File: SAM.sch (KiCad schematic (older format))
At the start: 63 parts

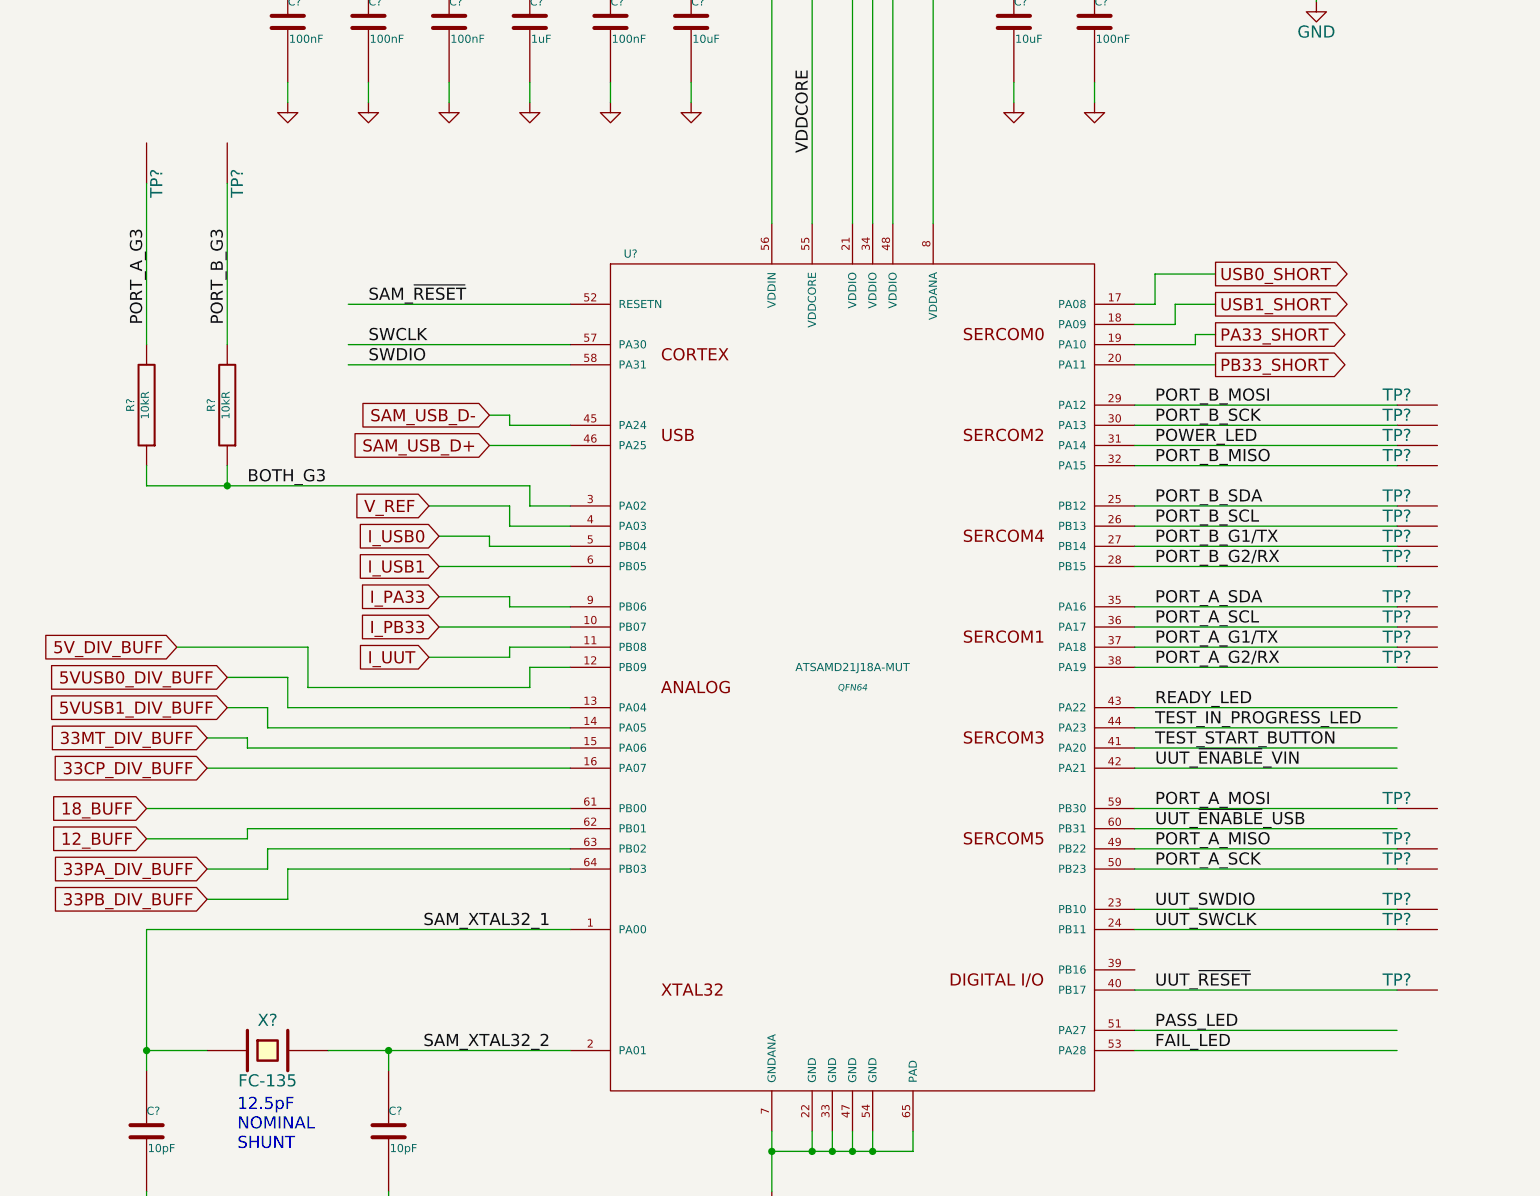
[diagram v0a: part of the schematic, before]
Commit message: added testpoint part number, small net naming changes
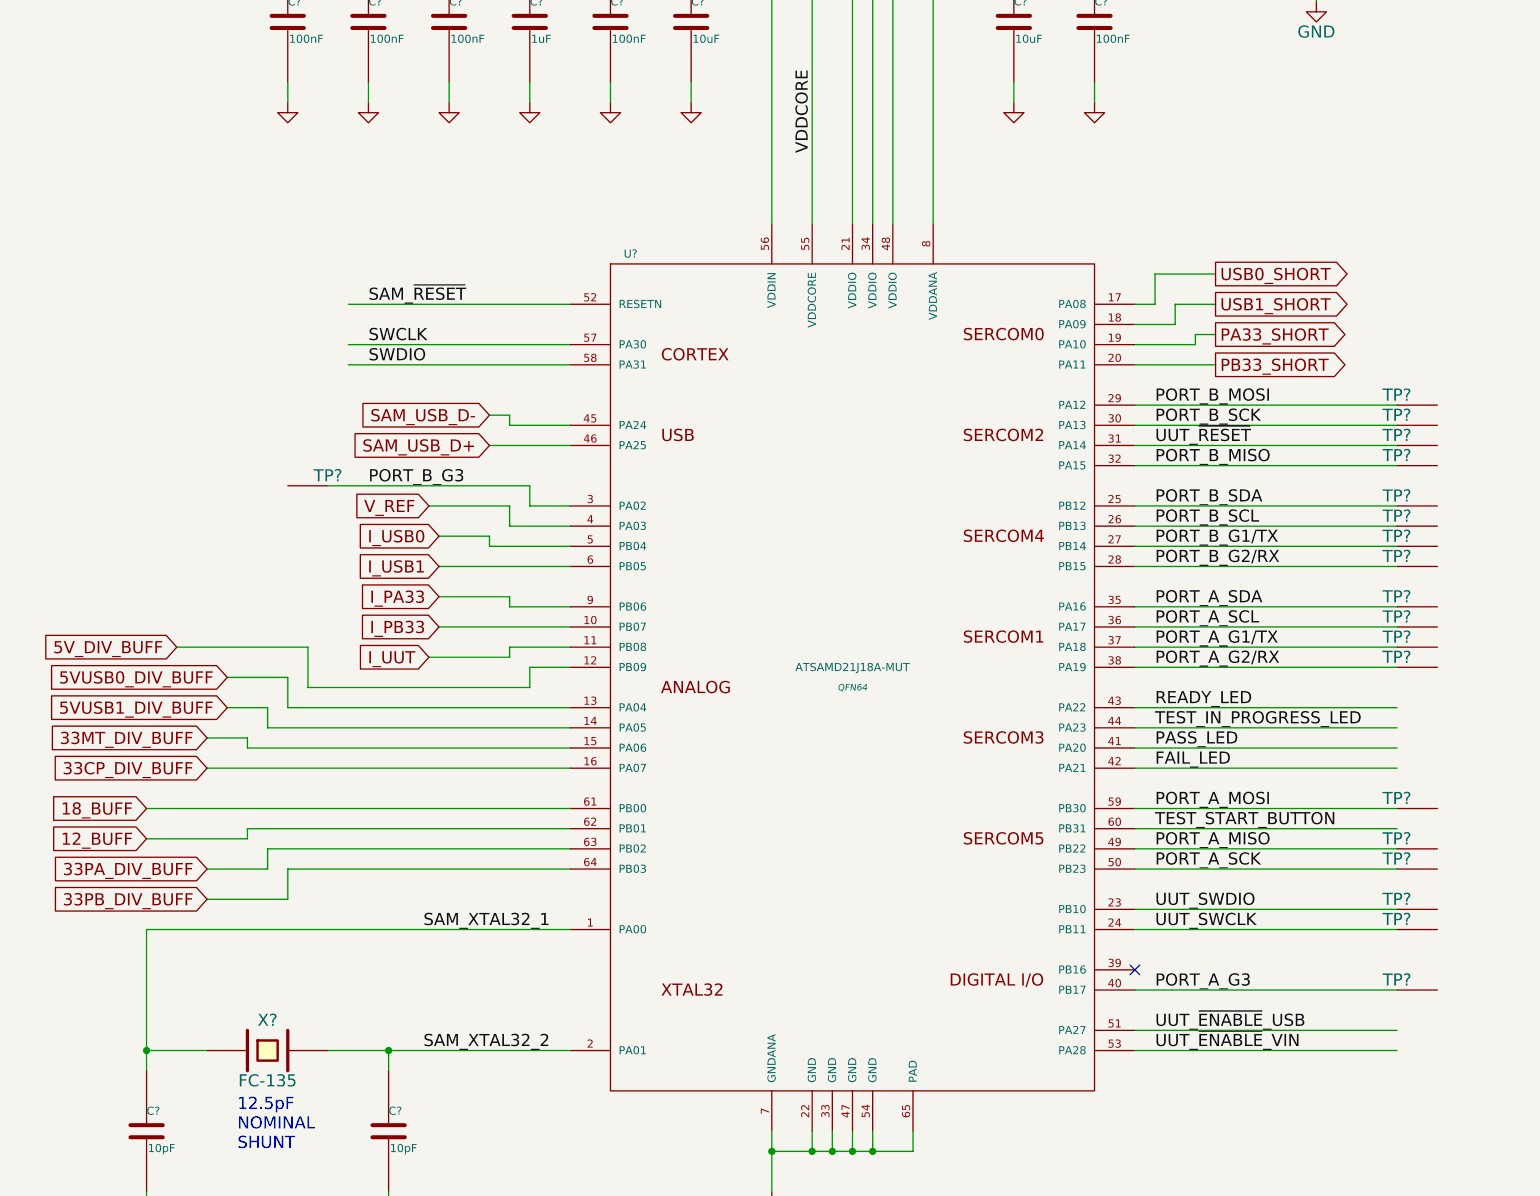
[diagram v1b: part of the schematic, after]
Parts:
- removed R? (x2): 10kR, tm-kicad-lib:SMD-0402-R, symbol TM_R
- removed TP?: TP, tm-kicad-lib:Testpoint, symbol TP
- TP? (x23): value TP -> 0914-0-15-20-77-14-11-0
- TP?: value TP -> 0914-0-15-20-77-14-11-0-0-15-20-77-14-11-0
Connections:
- net labels removed: BOTH_G3, POWER_LED
- wire segments 246 -> 241
- no-connect marks 4 -> 5
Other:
- moved on the sheet: TP?
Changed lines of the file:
@@
 Text Label 6800 6300 0    60   ~ 0
 PORT_B_G2/RX
-Text Label 2200 5100 1    60   ~ 0
+Text Label 2900 5900 0    60   ~ 0
 PORT_B_G3
 Text Label 6800 7500 0    60   ~ 0
@@
 Text Label 6800 6800 0    60   ~ 0
 PORT_A_G2/RX
-Text Label 6800 5700 0    60   ~ 0
-POWER_LED
 Text Notes 2250 9200 0    60   ~ 0
 12.5pF\nNOMINAL\nSHUNT
@@
 P 8800 2300
 F 0 "TP?" H 8800 2350 60  0000 C CNN
-F 1 "TP" H 8800 2250 60  0001 C CNN
+F 1 "0914-0-15-20-77-14-11-0" H 8800 2250 60  0001 C CNN
 F 2 "tm-kicad-lib:Testpoint" H 8800 2300 60  0001 C CNN
 F 3 "" H 8800 2300 60  0000 C CNN
@@
 P 8800 2500
 F 0 "TP?" H 8800 2550 60  0000 C CNN
-F 1 "TP" H 8800 2450 60  0001 C CNN
+F 1 "0914-0-15-20-77-14-11-0" H 8800 2450 60  0001 C CNN
 F 2 "tm-kicad-lib:Testpoint" H 8800 2500 60  0001 C CNN
 F 3 "" H 8800 2500 60  0000 C CNN
@@
 P 8800 2100
 F 0 "TP?" H 8800 2150 60  0000 C CNN
-F 1 "TP" H 8800 2050 60  0001 C CNN
+F 1 "0914-0-15-20-77-14-11-0" H 8800 2050 60  0001 C CNN
 F 2 "tm-kicad-lib:Testpoint" H 8800 2100 60  0001 C CNN
 F 3 "" H 8800 2100 60  0000 C CNN
@@
 P 8800 1900
 F 0 "TP?" H 8800 1950 60  0000 C CNN
-F 1 "TP" H 8800 1850 60  0001 C CNN
+F 1 "0914-0-15-20-77-14-11-0" H 8800 1850 60  0001 C CNN
 F 2 "tm-kicad-lib:Testpoint" H 8800 1900 60  0001 C CNN
 F 3 "" H 8800 1900 60  0000 C CNN
@@
 P 8000 5500
 F 0 "TP?" H 8000 5550 60  0000 C CNN
-F 1 "TP" H 8000 5450 60  0001 C CNN
+F 1 "0914-0-15-20-77-14-11-0-0-15-20-77-14-11-0" H 8000 5450 60  0001 C CNN
 F 2 "tm-kicad-lib:Testpoint" H 8000 5500 60  0001 C CNN
 F 3 "" H 8000 5500 60  0000 C CNN
@@
 P 8000 5600
 F 0 "TP?" H 8000 5650 60  0000 C CNN
-F 1 "TP" H 8000 5550 60  0001 C CNN
+F 1 "0914-0-15-20-77-14-11-0" H 8000 5550 60  0001 C CNN
 F 2 "tm-kicad-lib:Testpoint" H 8000 5600 60  0001 C CNN
 F 3 "" H 8000 5600 60  0000 C CNN
@@
 $Comp
 L TP TP?
-U 1 1 553FEFB0
-P 8000 5700
-F 0 "TP?" H 8000 5750 60  0000 C CNN
-F 1 "TP" H 8000 5650 60  0001 C CNN
-F 2 "tm-kicad-lib:Testpoint" H 8000 5700 60  0001 C CNN
-F 3 "" H 8000 5700 60  0000 C CNN
-	1    8000 5700
-	1    0    0    -1
-$EndComp
-$Comp
-L TP TP?
 U 1 1 553FEFB6
 P 8000 5800
 F 0 "TP?" H 8000 5850 60  0000 C CNN
-F 1 "TP" H 8000 5750 60  0001 C CNN
+F 1 "0914-0-15-20-77-14-11-0" H 8000 5750 60  0001 C CNN
 F 2 "tm-kicad-lib:Testpoint" H 8000 5800 60  0001 C CNN
 F 3 "" H 8000 5800 60  0000 C CNN
@@
 P 8000 6000
 F 0 "TP?" H 8000 6050 60  0000 C CNN
-F 1 "TP" H 8000 5950 60  0001 C CNN
+F 1 "0914-0-15-20-77-14-11-0" H 8000 5950 60  0001 C CNN
 F 2 "tm-kicad-lib:Testpoint" H 8000 6000 60  0001 C CNN
 F 3 "" H 8000 6000 60  0000 C CNN
@@
 P 8000 6100
 F 0 "TP?" H 8000 6150 60  0000 C CNN
-F 1 "TP" H 8000 6050 60  0001 C CNN
+F 1 "0914-0-15-20-77-14-11-0" H 8000 6050 60  0001 C CNN
 F 2 "tm-kicad-lib:Testpoint" H 8000 6100 60  0001 C CNN
 F 3 "" H 8000 6100 60  0000 C CNN
@@
 P 8000 6200
 F 0 "TP?" H 8000 6250 60  0000 C CNN
-F 1 "TP" H 8000 6150 60  0001 C CNN
+F 1 "0914-0-15-20-77-14-11-0" H 8000 6150 60  0001 C CNN
 F 2 "tm-kicad-lib:Testpoint" H 8000 6200 60  0001 C CNN
 F 3 "" H 8000 6200 60  0000 C CNN
@@
 P 8000 6300
 F 0 "TP?" H 8000 6350 60  0000 C CNN
-F 1 "TP" H 8000 6250 60  0001 C CNN
+F 1 "0914-0-15-20-77-14-11-0" H 8000 6250 60  0001 C CNN
 F 2 "tm-kicad-lib:Testpoint" H 8000 6300 60  0001 C CNN
 F 3 "" H 8000 6300 60  0000 C CNN
@@
 P 8000 6500
 F 0 "TP?" H 8000 6550 60  0000 C CNN
-F 1 "TP" H 8000 6450 60  0001 C CNN
+F 1 "0914-0-15-20-77-14-11-0" H 8000 6450 60  0001 C CNN
 F 2 "tm-kicad-lib:Testpoint" H 8000 6500 60  0001 C CNN
 F 3 "" H 8000 6500 60  0000 C CNN
@@
 P 8000 6600
 F 0 "TP?" H 8000 6650 60  0000 C CNN
-F 1 "TP" H 8000 6550 60  0001 C CNN
+F 1 "0914-0-15-20-77-14-11-0" H 8000 6550 60  0001 C CNN
 F 2 "tm-kicad-lib:Testpoint" H 8000 6600 60  0001 C CNN
 F 3 "" H 8000 6600 60  0000 C CNN
@@
 P 8000 6700
 F 0 "TP?" H 8000 6750 60  0000 C CNN
-F 1 "TP" H 8000 6650 60  0001 C CNN
+F 1 "0914-0-15-20-77-14-11-0" H 8000 6650 60  0001 C CNN
 F 2 "tm-kicad-lib:Testpoint" H 8000 6700 60  0001 C CNN
 F 3 "" H 8000 6700 60  0000 C CNN
@@
 P 8000 6800
 F 0 "TP?" H 8000 6850 60  0000 C CNN
-F 1 "TP" H 8000 6750 60  0001 C CNN
+F 1 "0914-0-15-20-77-14-11-0" H 8000 6750 60  0001 C CNN
 F 2 "tm-kicad-lib:Testpoint" H 8000 6800 60  0001 C CNN
 F 3 "" H 8000 6800 60  0000 C CNN
@@
 P 8000 8000
 F 0 "TP?" H 8000 8050 60  0000 C CNN
-F 1 "TP" H 8000 7950 60  0001 C CNN
+F 1 "0914-0-15-20-77-14-11-0" H 8000 7950 60  0001 C CNN
 F 2 "tm-kicad-lib:Testpoint" H 8000 8000 60  0001 C CNN
 F 3 "" H 8000 8000 60  0000 C CNN
@@
 P 8000 8100
 F 0 "TP?" H 8000 8150 60  0000 C CNN
-F 1 "TP" H 8000 8050 60  0001 C CNN
+F 1 "0914-0-15-20-77-14-11-0" H 8000 8050 60  0001 C CNN
 F 2 "tm-kicad-lib:Testpoint" H 8000 8100 60  0001 C CNN
 F 3 "" H 8000 8100 60  0000 C CNN
@@
 P 8000 7700
 F 0 "TP?" H 8000 7750 60  0000 C CNN
-F 1 "TP" H 8000 7650 60  0001 C CNN
+F 1 "0914-0-15-20-77-14-11-0" H 8000 7650 60  0001 C CNN
 F 2 "tm-kicad-lib:Testpoint" H 8000 7700 60  0001 C CNN
 F 3 "" H 8000 7700 60  0000 C CNN
@@
 P 8000 7800
 F 0 "TP?" H 8000 7850 60  0000 C CNN
-F 1 "TP" H 8000 7750 60  0001 C CNN
+F 1 "0914-0-15-20-77-14-11-0" H 8000 7750 60  0001 C CNN
 F 2 "tm-kicad-lib:Testpoint" H 8000 7800 60  0001 C CNN
 F 3 "" H 8000 7800 60  0000 C CNN
@@
 P 8000 7500
 F 0 "TP?" H 8000 7550 60  0000 C CNN
-F 1 "TP" H 8000 7450 60  0001 C CNN
+F 1 "0914-0-15-20-77-14-11-0" H 8000 7450 60  0001 C CNN
 F 2 "tm-kicad-lib:Testpoint" H 8000 7500 60  0001 C CNN
 F 3 "" H 8000 7500 60  0000 C CNN
@@
 	1    0    0    -1
 $EndComp
-Text Label 6800 8400 0    60   ~ 0
+Text Label 6800 5700 0    60   ~ 0
 UUT_~RESET
 $Comp
 L TP TP?
 U 1 1 553FFED4
-P 2200 4400
-F 0 "TP?" H 2200 4450 60  0000 C CNN
-F 1 "TP" H 2200 4350 60  0001 C CNN
-F 2 "tm-kicad-lib:Testpoint" H 2200 4400 60  0001 C CNN
-F 3 "" H 2200 4400 60  0000 C CNN
-	1    2200 4400
-	0    1    -1   0
+P 2700 5900
+F 0 "TP?" H 2700 5950 60  0000 C CNN
+F 1 "0914-0-15-20-77-14-11-0" H 2700 5850 60  0001 C CNN
+F 2 "tm-kicad-lib:Testpoint" H 2700 5900 60  0001 C CNN
+F 3 "" H 2700 5900 60  0000 C CNN
+	1    2700 5900
+	-1   0    0    -1
 $EndComp
 Text GLabel 7100 4850 2    60   Output ~ 0
@@
 L TP TP?
 U 1 1 5542FA8D
-P 8000 8400
-F 0 "TP?" H 8000 8450 60  0000 C CNN
-F 1 "TP" H 8000 8350 60  0001 C CNN
-F 2 "tm-kicad-lib:Testpoint" H 8000 8400 60  0001 C CNN
-F 3 "" H 8000 8400 60  0000 C CNN
-	1    8000 8400
+P 8000 5700
+F 0 "TP?" H 8000 5750 60  0000 C CNN
+F 1 "0914-0-15-20-77-14-11-0" H 8000 5650 60  0001 C CNN
+F 2 "tm-kicad-lib:Testpoint" H 8000 5700 60  0001 C CNN
+F 3 "" H 8000 5700 60  0000 C CNN
+	1    8000 5700
 	1    0    0    -1
 $EndComp
@@
 	1    0    0    -1
 $EndComp
-Text Label 6800 7600 0    60   ~ 0
+Text Label 6800 8600 0    60   ~ 0
 UUT_~ENABLE~_USB
 Text Label 13400 5500 2    60   ~ 0
@@
 Text GLabel 15600 5400 2    60   Output ~ 0
 UUT_VINUSB
-Text Label 6800 7300 0    60   ~ 0
+Text Label 6800 8700 0    60   ~ 0
 UUT_~ENABLE~_VIN
 $Comp
@@
 P 16100 6800
 F 0 "TP?" H 16100 6850 60  0000 C CNN
-F 1 "TP" H 16100 6750 60  0001 C CNN
+F 1 "0914-0-15-20-77-14-11-0" H 16100 6750 60  0001 C CNN
 F 2 "" H 16100 6800 60  0000 C CNN
 F 3 "" H 16100 6800 60  0000 C CNN
@@
 	8000 8000 6700 8000
 Connection ~ 6500 3200
-Wire Wire Line
-	6700 5700 8000 5700
 Connection ~ 7600 3100
 Wire Wire Line
@@
 	8000 8100 6700 8100
 Wire Wire Line
-	1800 5900 2200 5900
-Wire Wire Line
-	2200 5900 3700 5900
+	2700 5900 3700 5900
 Wire Wire Line
 	3700 5900 3700 6000
@@
 	2500 7800 3900 7800
 Wire Wire Line
-	8000 8400 6700 8400
+	8000 5700 6700 5700
 Wire Wire Line
 	3900 6200 3500 6200
@@
 	16100 7100 16100 6800
 Connection ~ 13800 5400
-$Comp
-L TM_R R?
-U 1 1 554415E8
-P 2200 5500
-F 0 "R?" V 2280 5500 40  0000 C CNN
-F 1 "10kR" V 2207 5501 40  0000 C CNN
-F 2 "tm-kicad-lib:SMD-0402-R" V 2130 5500 30  0001 C CNN
-F 3 "" H 2200 5500 30  0000 C CNN
-	1    2200 5500
-	-1   0    0    1
-$EndComp
-Wire Wire Line
-	2200 4400 2200 5200
-Wire Wire Line
-	1800 5900 1800 5800
-Wire Wire Line
-	2200 5800 2200 5900
-Connection ~ 2200 5900
-Text Label 1800 5100 1    60   ~ 0
+Text Label 6800 8400 0    60   ~ 0
 PORT_A_G3
 $Comp
 L TP TP?
 U 1 1 55441C97
-P 1800 4400
-F 0 "TP?" H 1800 4450 60  0000 C CNN
-F 1 "TP" H 1800 4350 60  0001 C CNN
-F 2 "tm-kicad-lib:Testpoint" H 1800 4400 60  0001 C CNN
-F 3 "" H 1800 4400 60  0000 C CNN
-	1    1800 4400
-	0    1    -1   0
-$EndComp
-$Comp
-L TM_R R?
-U 1 1 55441C9D
-P 1800 5500
-F 0 "R?" V 1880 5500 40  0000 C CNN
-F 1 "10kR" V 1807 5501 40  0000 C CNN
-F 2 "tm-kicad-lib:SMD-0402-R" V 1730 5500 30  0001 C CNN
-F 3 "" H 1800 5500 30  0000 C CNN
-	1    1800 5500
-	-1   0    0    1
-$EndComp
-Wire Wire Line
-	1800 4400 1800 5200
-Text Label 2300 5900 0    60   ~ 0
-BOTH_G3
+P 8000 8400
+F 0 "TP?" H 8000 8450 60  0000 C CNN
+F 1 "0914-0-15-20-77-14-11-0" H 8000 8350 60  0001 C CNN
+F 2 "tm-kicad-lib:Testpoint" H 8000 8400 60  0001 C CNN
+F 3 "" H 8000 8400 60  0000 C CNN
+	1    8000 8400
+	1    0    0    -1
+$EndComp
 Wire Wire Line
 	2600 6900 2600 6700
@@
 Text Label 6800 7100 0    60   ~ 0
 TEST_IN_PROGRESS_LED
-Text Label 6800 8600 0    60   ~ 0
+Text Label 6800 7200 0    60   ~ 0
 PASS_LED
-Text Label 6800 8700 0    60   ~ 0
+Text Label 6800 7300 0    60   ~ 0
 FAIL_LED
-Text Label 6800 7200 0    60   ~ 0
+Text Label 6800 7600 0    60   ~ 0
 TEST_START_BUTTON
 Wire Wire Line
@@
 Text Label 11600 2400 0    60   ~ 0
 TEST_START_BUTTON
+NoConn ~ 6700 8300
+Wire Wire Line
+	6700 8400 8000 8400
 $EndSCHEMATC

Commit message: annotated
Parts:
- gave numbers to parts that had none: 60

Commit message: annotated, netlist
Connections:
- wire segments 241 -> 206
